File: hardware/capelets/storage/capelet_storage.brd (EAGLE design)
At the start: 16.5 x 12.7 mm, 4 parts

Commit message: hardware: updated capelets
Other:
- board text added: "SHPRD v1.4 CPLT STRG"
- board text removed: "SHPRD v1.3 CPLT STRG"
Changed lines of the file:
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@@
 <dimension x1="17.145" y1="12.7" x2="17.145" y2="0" x3="20.32" y3="6.35" textsize="1.143" textratio="16" layer="47"/>
 <dimension x1="0.635" y1="12.7" x2="17.145" y2="12.7" x3="8.89" y3="13.97" textsize="1.143" textratio="16" layer="47"/>
-<text x="2.286" y="11.684" size="0.889" layer="25" font="vector" ratio="16">SHPRD v1.3 CPLT STRG</text>
+<text x="2.286" y="11.684" size="0.889" layer="25" font="vector" ratio="16">SHPRD v1.4 CPLT STRG</text>
 </plain>
 <attributes>
@@
 <element name="U$1" library="shepherd" package="SHPRD_CPLT_S" value="SHPRD_CPLT_S" x="0" y="0" smashed="yes"/>
 <element name="C1" library="shepherd" package="CAPC2012X145" package3d_urn="urn:adsk.eagle:package:4930364/1" value="" x="8.89" y="10.16" smashed="yes">
-<attribute name="NAME" x="6.985" y="8.7876" size="1.016" layer="25" font="vector" ratio="16" align="bottom-center"/>
+<attribute name="NAME" x="6.731" y="8.5336" size="1.016" layer="25" font="vector" ratio="16" align="bottom-center"/>
 <attribute name="VALUE" x="8.89" y="8.4844" size="1.27" layer="27" align="top-center"/>
 </element>
@@
 </element>
 <element name="C3" library="rcl" library_urn="urn:adsk.eagle:library:334" package="E5-8,5" package3d_urn="urn:adsk.eagle:package:23374/1" value="" x="8.89" y="6.35" smashed="yes">
-<attribute name="NAME" x="10.1092" y="7.747" size="1.016" layer="25" font="vector" ratio="16"/>
+<attribute name="NAME" x="10.8712" y="7.874" size="1.016" layer="25" font="vector" ratio="16"/>
 <attribute name="SPICEPREFIX" value="C" x="8.89" y="6.35" size="1.778" layer="27" display="off"/>
 <attribute name="VALUE" x="6.3754" y="3.3274" size="1.27" layer="27" ratio="10"/>

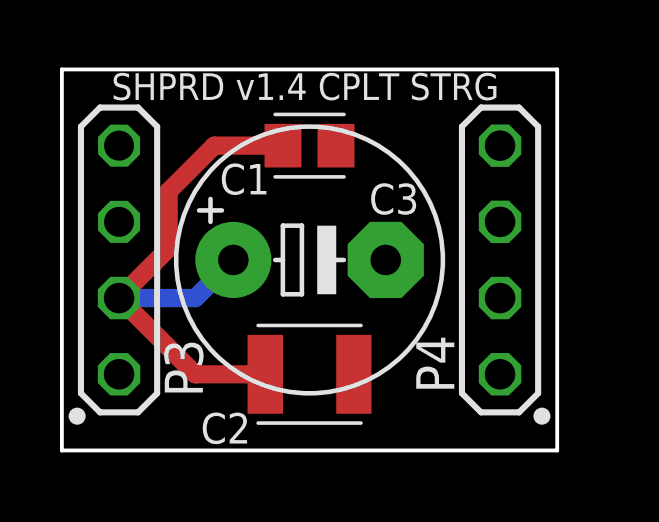
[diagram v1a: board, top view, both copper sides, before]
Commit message: hardware: prepared capelets for external manufacturing
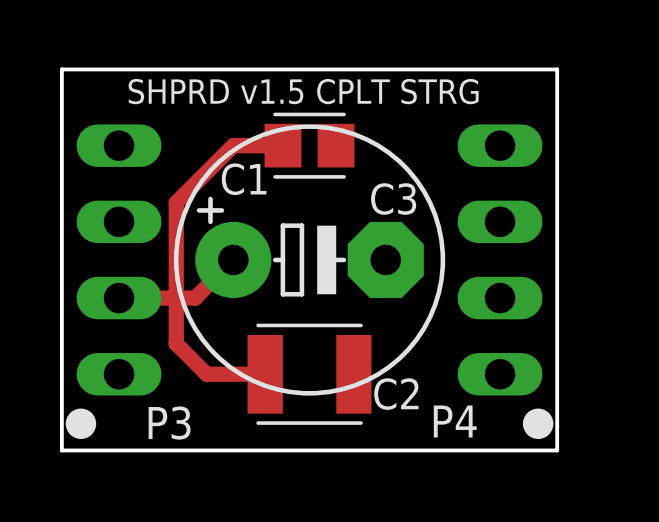
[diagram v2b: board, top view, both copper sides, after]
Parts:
- added P3, P4: (no value), pinhead:1X04
- U$1: value SHPRD_CPLT_S -> (none)
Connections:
- net +3V3: now also P3.1; no longer U$1.P$1
- net GND: now also P3.3, P3.4, P4.1, P4.2, P4.3, P4.4; no longer U$1.P$3, U$1.P$4, U$1.P$5, U$1.P$6, U$1.P$7, U$1.P$8
- net N$1: now also P3.2; no longer U$1.P$2
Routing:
- net N$1: track 18.9 -> 16.8 mm
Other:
- board text added: "P3: Pins pointing to bottom, solder on top"
- board text added: "P4: Pins pointing to bottom, solder on top"
- board text added: "SHPRD v1.5 CPLT STRG"
- board text removed: "SHPRD v1.4 CPLT STRG"
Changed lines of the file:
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@@
 <?xml version="1.0" encoding="utf-8"?>
 <!DOCTYPE eagle SYSTEM "eagle.dtd">
-<eagle version="9.4.2">
+<eagle version="9.5.2">
 <drawing>
 <settings>
@@
 <layers>
 <layer number="1" name="Top" color="4" fill="1" visible="yes" active="yes"/>
-<layer number="2" name="Route2" color="16" fill="1" visible="no" active="yes"/>
+<layer number="2" name="Route2" color="16" fill="1" visible="no" active="no"/>
 <layer number="3" name="Route3" color="17" fill="1" visible="no" active="no"/>
 <layer number="4" name="Route4" color="18" fill="1" visible="no" active="no"/>
@@
 <layer number="13" name="Route13" color="21" fill="1" visible="no" active="no"/>
 <layer number="14" name="Route14" color="22" fill="1" visible="no" active="no"/>
-<layer number="15" name="Route15" color="23" fill="1" visible="no" active="yes"/>
+<layer number="15" name="Route15" color="23" fill="1" visible="no" active="no"/>
 <layer number="16" name="Bottom" color="1" fill="1" visible="yes" active="yes"/>
 <layer number="17" name="Pads" color="2" fill="1" visible="yes" active="yes"/>
@@
 <dimension x1="17.145" y1="12.7" x2="17.145" y2="0" x3="20.32" y3="6.35" textsize="1.143" textratio="16" layer="47"/>
 <dimension x1="0.635" y1="12.7" x2="17.145" y2="12.7" x3="8.89" y3="13.97" textsize="1.143" textratio="16" layer="47"/>
-<text x="2.286" y="11.684" size="0.889" layer="25" font="vector" ratio="16">SHPRD v1.4 CPLT STRG</text>
+<text x="2.794" y="11.557" size="0.8128" layer="25" font="vector" ratio="16">SHPRD v1.5 CPLT STRG</text>
+<circle x="1.27" y="0.889" radius="0.254" width="0.508" layer="21"/>
+<circle x="16.51" y="0.889" radius="0.254" width="0.508" layer="21"/>
+<text x="21.082" y="11.811" size="1.016" layer="48" font="vector" ratio="17" rot="R270">P4: Pins pointing
+to bottom,
+solder on top</text>
+<text x="-3.937" y="13.081" size="1.016" layer="48" font="vector" ratio="17" rot="R270">P3: Pins pointing
+to bottom,
+solder on top</text>
 </plain>
 <attributes>
@@
 </class>
 </classes>
-<designrules name="PCB-POOL Standard_ML4">
+<designrules name="PCB-POOL Standard">
 <description language="de">&lt;b&gt;EAGLE Design Rules Prototypen  für PCB-POOL(R)&lt;/b&gt;
 &lt;p&gt;
@@
 Covered vias can be set in Masks (Limit).
 &lt;/p&gt;Your Beta LAYOUT Team</description>
-<param name="layerSetup" value="(1+2*15+16)"/>
+<param name="layerSetup" value="(1*16)"/>
 <param name="mtCopper" value="0.035mm 0.035mm 0.035mm 0.035mm 0.035mm 0.035mm 0.035mm 0.035mm 0.035mm 0.035mm 0.035mm 0.035mm 0.035mm 0.035mm 0.035mm 0.035mm"/>
-<param name="mtIsolate" value="0.38mm 0.71mm 0.38mm 0.15mm 0.2mm 0.15mm 0.2mm 0.15mm 0.2mm 0.15mm 0.2mm 0.15mm 0.2mm 0.15mm 0.38mm"/>
+<param name="mtIsolate" value="1.5mm 0.15mm 0.2mm 0.15mm 0.2mm 0.15mm 0.2mm 0.15mm 0.2mm 0.15mm 0.2mm 0.15mm 0.2mm 0.15mm 0.2mm"/>
 <param name="mdWireWire" value="0.15mm"/>
 <param name="mdWirePad" value="0.15mm"/>
@@
 <param name="mvStopFrame" value="0"/>
 <param name="mvCreamFrame" value="0"/>
-<param name="mlMinStopFrame" value="0.075mm"/>
+<param name="mlMinStopFrame" value="0.03mm"/>
 <param name="mlMaxStopFrame" value="0.2mm"/>
 <param name="mlMinCreamFrame" value="0mil"/>
@@
 </autorouter>
 <elements>
-<element name="U$1" library="shepherd" package="SHPRD_CPLT_S" value="SHPRD_CPLT_S" x="0" y="0" smashed="yes"/>
 <element name="C1" library="shepherd" package="CAPC2012X145" package3d_urn="urn:adsk.eagle:package:4930364/1" value="" x="8.89" y="10.16" smashed="yes">
 <attribute name="NAME" x="6.731" y="8.5336" size="1.016" layer="25" font="vector" ratio="16" align="bottom-center"/>
@@
 </element>
 <element name="C2" library="shepherd" package="CAPC3225X280" package3d_urn="urn:adsk.eagle:package:4926069/1" value="" x="8.89" y="2.54" smashed="yes">
-<attribute name="NAME" x="6.096" y="0.2296" size="1.016" layer="25" font="vector" ratio="16" align="bottom-center"/>
+<attribute name="NAME" x="11.811" y="1.3726" size="1.016" layer="25" font="vector" ratio="16" align="bottom-center"/>
 <attribute name="VALUE" x="8.89" y="0.2784" size="1.27" layer="27" align="top-center"/>
 </element>
@@
 <attribute name="VALUE" x="6.3754" y="3.3274" size="1.27" layer="27" ratio="10"/>
 </element>
+<element name="P4" library="pinhead" library_urn="urn:adsk.eagle:library:325" package="1X04" package3d_urn="urn:adsk.eagle:package:22407/2" value="" x="15.24" y="6.35" smashed="yes" rot="MR90">
+<attribute name="NAME" x="12.9032" y="0.4318" size="1.0668" layer="25" font="vector" ratio="17"/>
+<attribute name="POPULARITY" value="91" x="15.24" y="6.35" size="1.778" layer="28" rot="MR90" display="off"/>
+<attribute name="VALUE" x="12.065" y="1.27" size="1.27" layer="28" rot="MR90"/>
+</element>
+<element name="P3" library="pinhead" library_urn="urn:adsk.eagle:library:325" package="1X04" package3d_urn="urn:adsk.eagle:package:22407/2" value="" x="2.54" y="6.35" smashed="yes" rot="MR90">
+<attribute name="NAME" x="5.0292" y="1.4478" size="1.0668" layer="25" font="vector" ratio="17" rot="R180"/>
+<attribute name="POPULARITY" value="91" x="2.54" y="6.35" size="1.778" layer="28" rot="MR90" display="off"/>
+<attribute name="VALUE" x="-0.635" y="1.27" size="1.27" layer="28" rot="MR90"/>
+</element>
+<element name="U$1" library="shepherd" package="SHPRD_CPLT_S" value="" x="0" y="0" smashed="yes"/>
 </elements>
 <signals>
-<signal name="+3V3">
-<contactref element="U$1" pad="P$1"/>
-</signal>
 <signal name="GND">
-<contactref element="U$1" pad="P$8"/>
-<contactref element="U$1" pad="P$7"/>
-<contactref element="U$1" pad="P$3"/>
-<contactref element="U$1" pad="P$4"/>
-<contactref element="U$1" pad="P$5"/>
-<contactref element="U$1" pad="P$6"/>
 <contactref element="C3" pad="-"/>
 <contactref element="C1" pad="2"/>
@@
 <vertex x="0.635" y="0"/>
 </polygon>
+<contactref element="P4" pad="4"/>
+<contactref element="P4" pad="3"/>
+<contactref element="P4" pad="2"/>
+<contactref element="P4" pad="1"/>
+<contactref element="P3" pad="3"/>
+<contactref element="P3" pad="4"/>
 </signal>
 <signal name="N$1">
 <contactref element="C2" pad="1"/>
-<contactref element="U$1" pad="P$2"/>
 <contactref element="C1" pad="1"/>
 <contactref element="C3" pad="+"/>
-<wire x1="2.54" y1="5.08" x2="5.08" y2="2.54" width="0.6096" layer="1"/>
-<wire x1="2.54" y1="5.08" x2="4.191" y2="6.731" width="0.6096" layer="1"/>
-<wire x1="4.191" y1="8.636" x2="5.715" y2="10.16" width="0.6096" layer="1"/>
-<wire x1="5.715" y1="10.16" x2="8.0057" y2="10.16" width="0.6096" layer="1"/>
-<wire x1="4.191" y1="6.731" x2="4.191" y2="8.636" width="0.6096" layer="1"/>
-<wire x1="5.08" y1="2.54" x2="7.4126" y2="2.54" width="0.6096" layer="1"/>
-<wire x1="2.54" y1="5.08" x2="5.08" y2="5.08" width="0.6096" layer="16"/>
-<wire x1="5.08" y1="5.08" x2="6.35" y2="6.35" width="0.6096" layer="16"/>
+<contactref element="P3" pad="2"/>
+<wire x1="2.54" y1="5.08" x2="4.445" y2="5.08" width="0.508" layer="1"/>
+<wire x1="4.445" y1="5.08" x2="5.08" y2="5.08" width="0.508" layer="1"/>
+<wire x1="5.08" y1="5.08" x2="6.35" y2="6.35" width="0.508" layer="1"/>
+<wire x1="8.0057" y1="10.16" x2="6.35" y2="10.16" width="0.508" layer="1"/>
+<wire x1="6.35" y1="10.16" x2="4.445" y2="8.255" width="0.508" layer="1"/>
+<wire x1="4.445" y1="8.255" x2="4.445" y2="5.08" width="0.508" layer="1"/>
+<wire x1="7.4126" y1="2.54" x2="5.461" y2="2.54" width="0.508" layer="1"/>
+<wire x1="4.445" y1="3.556" x2="4.445" y2="5.08" width="0.508" layer="1"/>
+<wire x1="5.461" y1="2.54" x2="4.445" y2="3.556" width="0.508" layer="1"/>
+</signal>
+<signal name="+3V3">
+<contactref element="P3" pad="1"/>
 </signal>
 </signals>
@@
 </drawing>
 <compatibility>
+<note version="6.3" minversion="6.2.2" severity="warning">
+Since Version 6.2.2 text objects can contain more than one line,
+which will not be processed correctly with this version.
+</note>
 <note version="8.2" severity="warning">
 Since Version 8.2, EAGLE supports online libraries. The ids
